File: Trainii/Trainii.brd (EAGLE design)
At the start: 50.8 x 71.1 mm, 31 parts, among them J1 apd, J2 left motor encoder, J3 right motor encoder, J4 line sensor 2, J5 line sensor 1, J6 ultrasonic, J7 left motor output, J8 right motor output, J9 lift motor output, U1 TPS61222DCKR, U2 BSS138

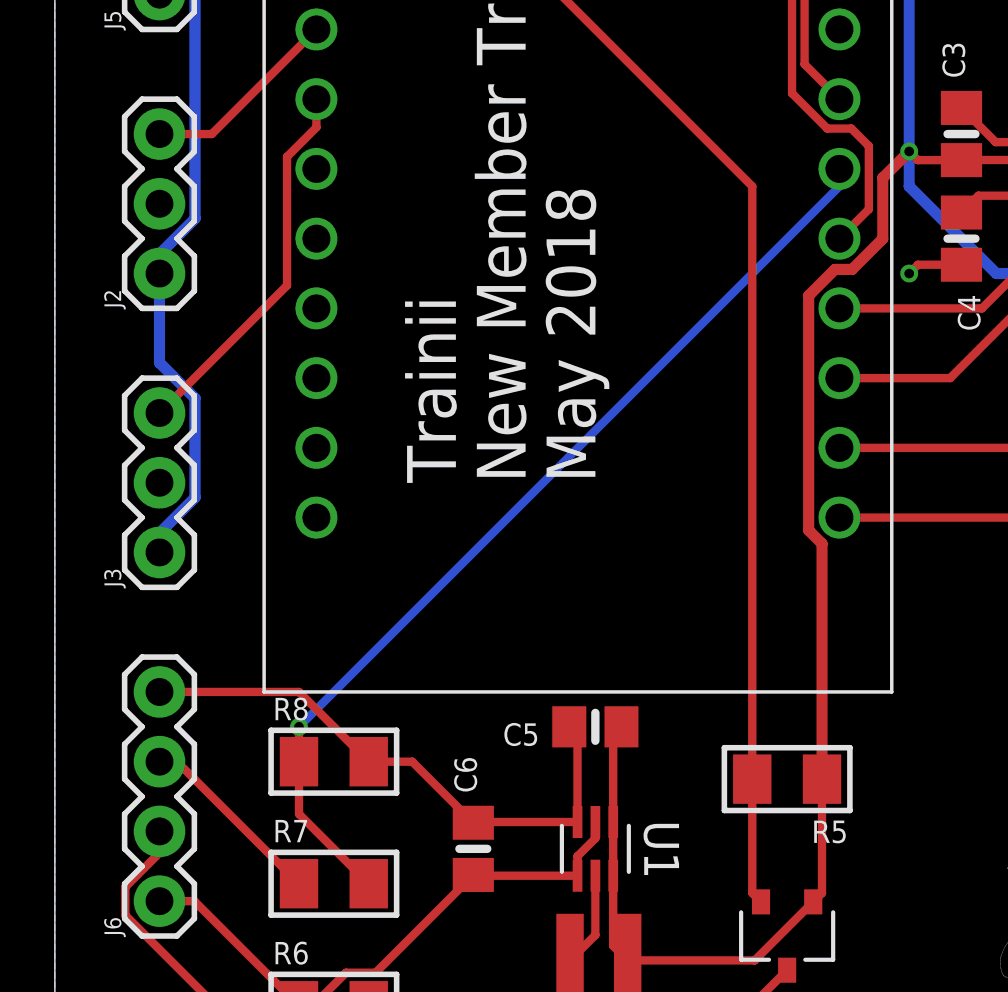
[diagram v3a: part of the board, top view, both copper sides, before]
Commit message: Fixes spacing between ECHO3.3 and R8
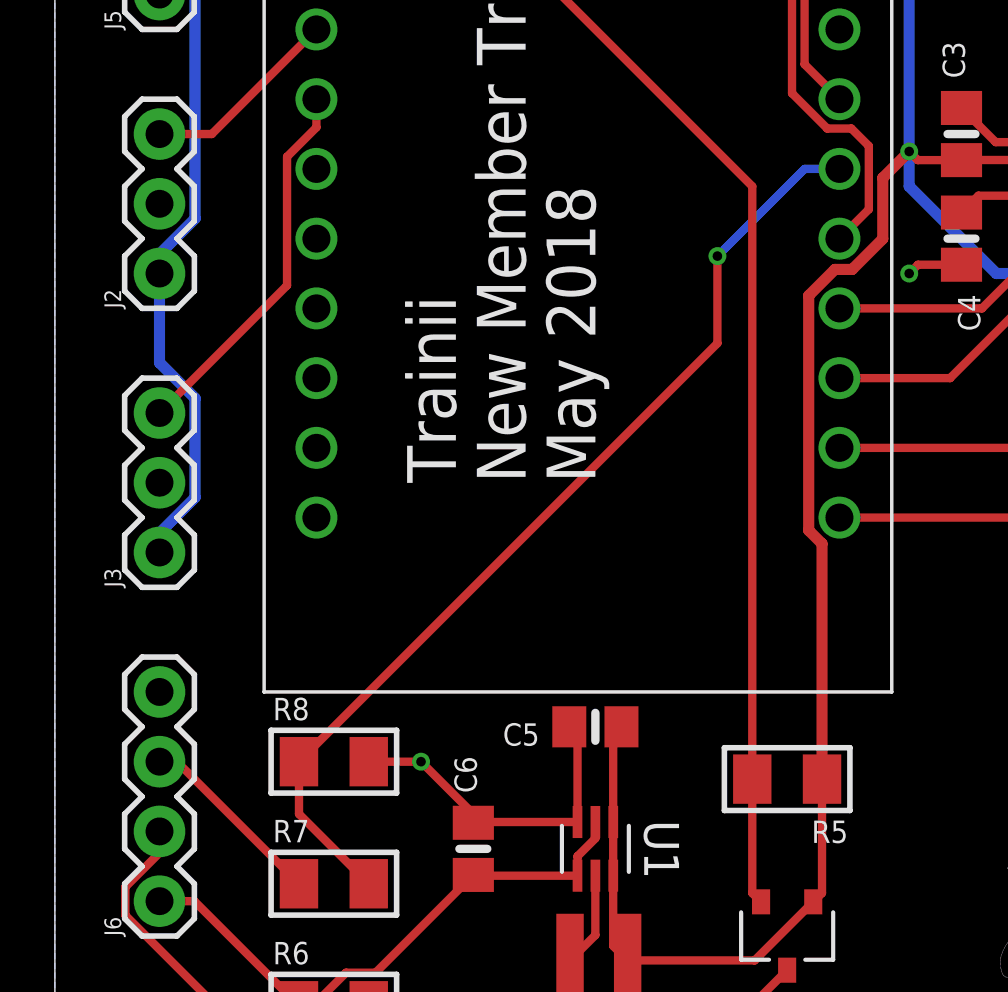
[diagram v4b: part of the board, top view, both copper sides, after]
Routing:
- net GND: track 55.1 -> 46.6 mm, vias 4 -> 5
- net ECHO3.3: track 35.2 -> 36.0 mm
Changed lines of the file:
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@@
 <wire x1="19.035" y1="15.5829" x2="19.035" y2="18.75" width="0.3048" layer="1"/>
 <wire x1="19.035" y1="18.75" x2="18.735" y2="19.05" width="0.3048" layer="1"/>
-<wire x1="15.24" y1="15.555" x2="13.015" y2="17.78" width="0.3048" layer="1"/>
-<wire x1="13.015" y1="17.78" x2="11.43" y2="17.78" width="0.3048" layer="1"/>
-<wire x1="11.43" y1="17.78" x2="8.89" y2="20.32" width="0.3048" layer="1"/>
-<wire x1="8.89" y1="20.32" x2="3.81" y2="20.32" width="0.3048" layer="1"/>
 <wire x1="39.37" y1="33.02" x2="39.37" y2="39.37" width="0.3048" layer="1"/>
 <wire x1="33.02" y1="56.2" x2="31.435" y2="56.2" width="0.3048" layer="1"/>
@@
 <wire x1="39.37" y1="62.865" x2="39.37" y2="66.04" width="0.3048" layer="1"/>
 <via x="39.37" y="62.865" extent="1-16" drill="0.35"/>
+<wire x1="11.43" y1="17.78" x2="13.335" y2="17.78" width="0.3048" layer="1"/>
+<via x="13.335" y="17.78" extent="1-16" drill="0.35"/>
+<wire x1="13.335" y1="17.78" x2="15.2679" y2="15.8471" width="0.3048" layer="1"/>
+<wire x1="15.2679" y1="15.8471" x2="15.2679" y2="15.5829" width="0.3048" layer="1"/>
 </signal>
 <signal name="N$3">
@@
 <wire x1="11.43" y1="13.335" x2="8.89" y2="15.875" width="0.3048" layer="1"/>
 <wire x1="8.89" y1="15.875" x2="8.89" y2="17.78" width="0.3048" layer="1"/>
-<wire x1="8.89" y1="17.78" x2="8.89" y2="19.05" width="0.3048" layer="1"/>
-<via x="8.89" y="19.05" extent="1-16" drill="0.35"/>
-<wire x1="8.89" y1="19.05" x2="28.575" y2="38.735" width="0.3048" layer="16"/>
-<wire x1="28.575" y1="38.735" x2="28.575" y2="39.37" width="0.3048" layer="16"/>
+<wire x1="8.89" y1="17.78" x2="24.13" y2="33.02" width="0.3048" layer="1"/>
+<wire x1="24.13" y1="33.02" x2="24.13" y2="36.195" width="0.3048" layer="1"/>
+<via x="24.13" y="36.195" extent="1-16" drill="0.35"/>
+<wire x1="24.13" y1="36.195" x2="27.305" y2="39.37" width="0.3048" layer="16"/>
+<wire x1="27.305" y1="39.37" x2="28.575" y2="39.37" width="0.3048" layer="16"/>
 </signal>
 <signal name="3V">

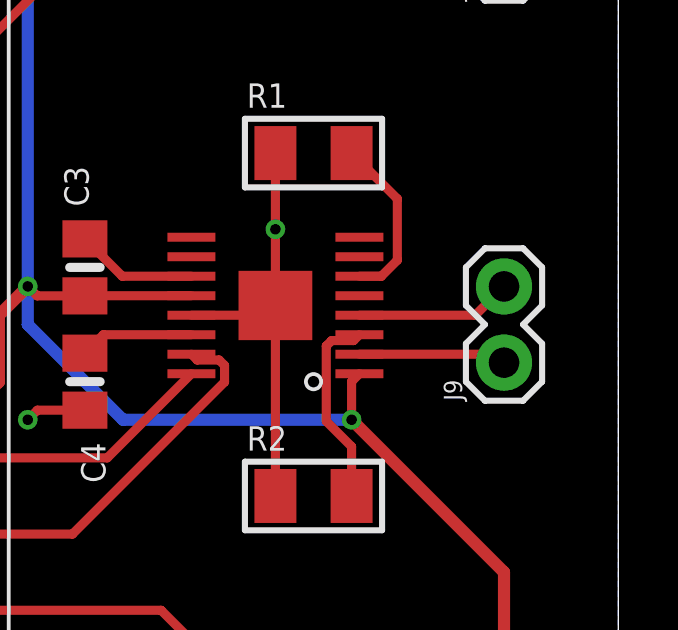
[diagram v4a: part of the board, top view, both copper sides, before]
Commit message: Fixes location of J9
It was slightly off of the 0.1" grid I tried to fit all of the connectors to.
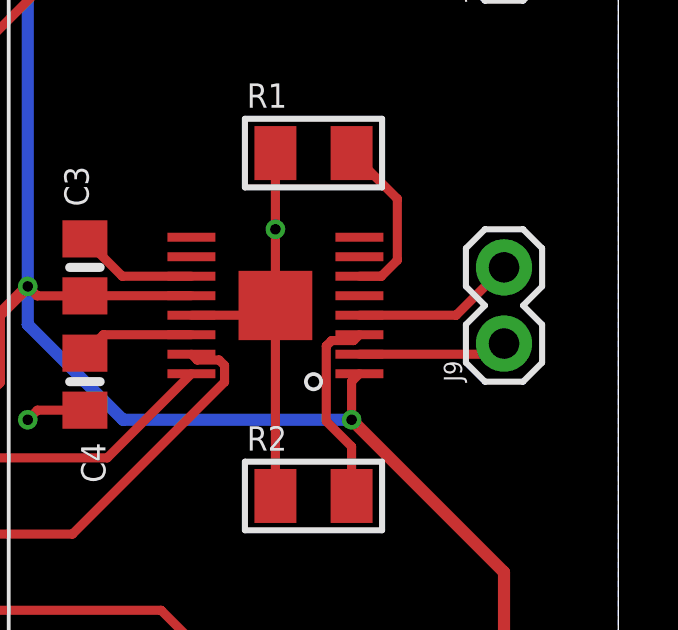
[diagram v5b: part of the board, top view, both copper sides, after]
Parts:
- moved J9 0.63 mm to (47.0, 38.1)
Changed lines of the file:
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@@
 <element name="J7" library="SparkFun-Connectors" library_urn="urn:adsk.eagle:library:513" package="1X02" package3d_urn="urn:adsk.eagle:package:38039/1" value="left motor output" x="46.99" y="50.8" rot="R90"/>
 <element name="J8" library="SparkFun-Connectors" library_urn="urn:adsk.eagle:library:513" package="1X02" package3d_urn="urn:adsk.eagle:package:38039/1" value="right motor output" x="46.99" y="58.42" rot="R90"/>
-<element name="J9" library="SparkFun-Connectors" library_urn="urn:adsk.eagle:library:513" package="1X02" package3d_urn="urn:adsk.eagle:package:38039/1" value="lift motor output" x="46.99" y="37.465" rot="R90"/>
+<element name="J9" library="SparkFun-Connectors" library_urn="urn:adsk.eagle:library:513" package="1X02" package3d_urn="urn:adsk.eagle:package:38039/1" value="lift motor output" x="46.99" y="38.1" rot="R90"/>
 <element name="MC2" library="Trainii" package="DRV8833" value="DRV8833" x="39.37" y="39.37" rot="R90"/>
 <element name="C3" library="microbuilder" package="0805-NO" value="0.1uF" x="33.02" y="40.64" rot="R90"/>
@@
 <contactref element="J9" pad="1"/>
 <contactref element="MC2" pad="AOUT1"/>
-<wire x1="42.17" y1="37.745" x2="46.71" y2="37.745" width="0.3048" layer="1"/>
-<wire x1="46.71" y1="37.745" x2="46.99" y2="37.465" width="0.3048" layer="1"/>
+<wire x1="42.17" y1="37.745" x2="46.635" y2="37.745" width="0.3048" layer="1"/>
+<wire x1="46.635" y1="37.745" x2="46.99" y2="38.1" width="0.3048" layer="1"/>
 </signal>
 <signal name="RIGHT_B">
@@
 <contactref element="MC2" pad="AOUT2"/>
 <contactref element="J9" pad="2"/>
-<wire x1="42.17" y1="39.045" x2="46.03" y2="39.045" width="0.3048" layer="1"/>
-<wire x1="46.03" y1="39.045" x2="46.99" y2="40.005" width="0.3048" layer="1"/>
+<wire x1="42.17" y1="39.045" x2="45.395" y2="39.045" width="0.3048" layer="1"/>
+<wire x1="45.395" y1="39.045" x2="46.99" y2="40.64" width="0.3048" layer="1"/>
 </signal>
 <signal name="RIGHT_0">

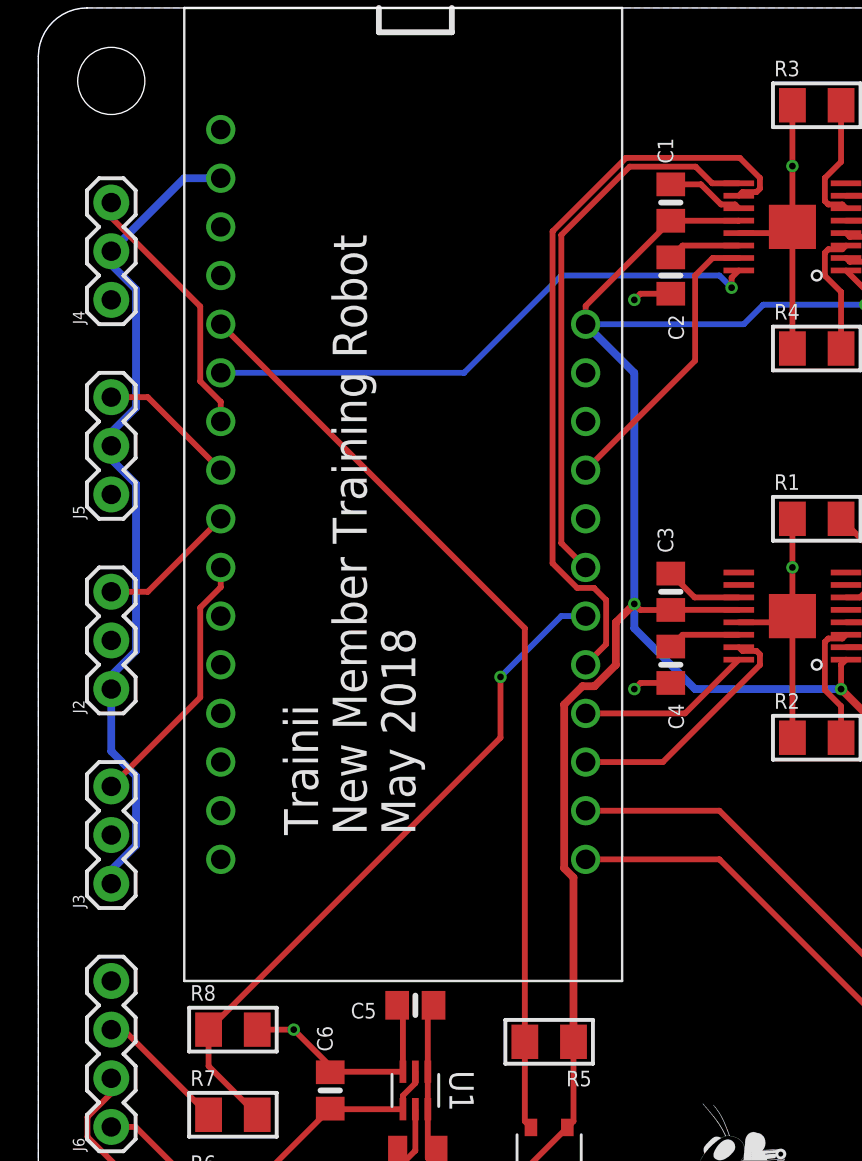
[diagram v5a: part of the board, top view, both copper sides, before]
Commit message: Fixes header spacing for the Huzzah ESP32 in Trainii.lbr
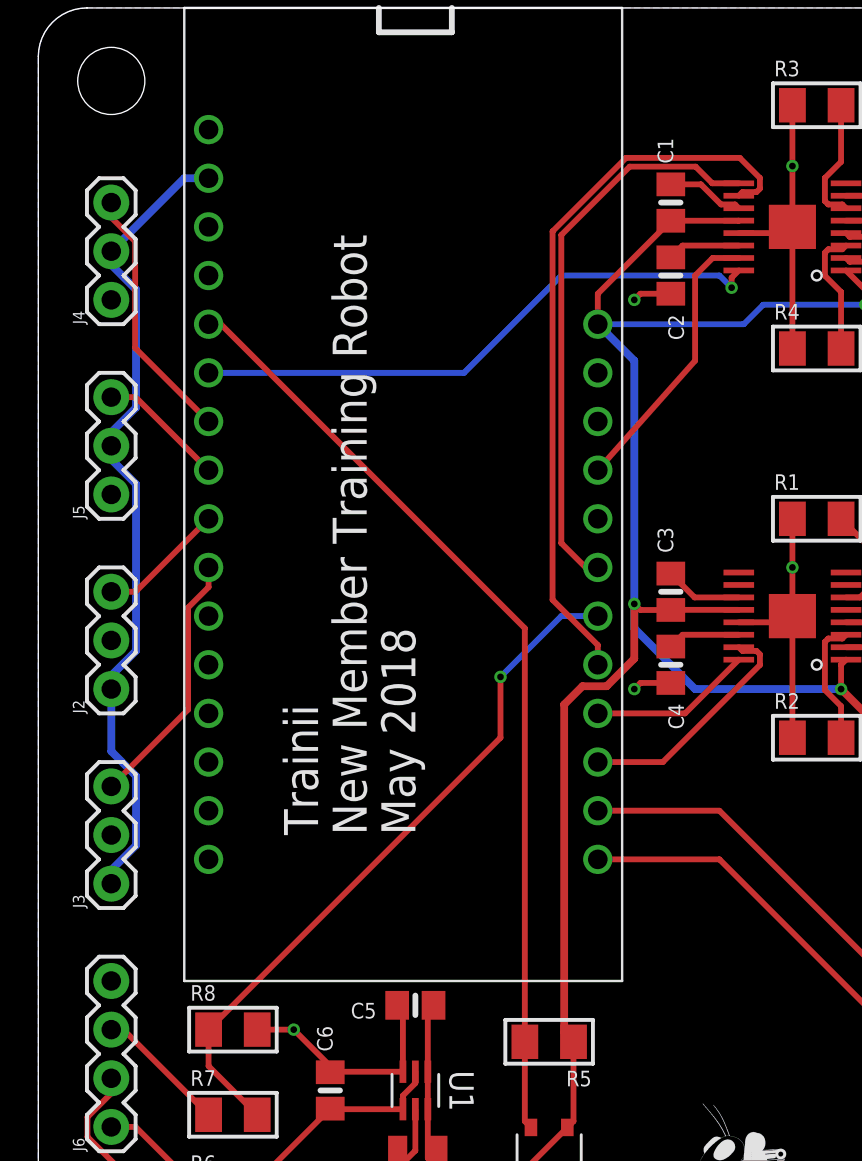
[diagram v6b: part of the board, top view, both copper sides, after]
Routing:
- net RIGHT_B: track 39.4 -> 38.3 mm
- net VCC: track 122.6 -> 121.8 mm
- net 3V: track 43.5 -> 42.9 mm
- net SDA: track 23.1 -> 22.5 mm
- net SCL: track 23.1 -> 22.5 mm
- net RIGHT_A: track 29.0 -> 29.6 mm
- net LIFT_B: track 13.0 -> 12.4 mm
- net LIFT_A: track 9.16 -> 8.52 mm
- net LEFT_A: track 30.1 -> 30.7 mm
- net TICK_LEFT: track 7.29 -> 6.66 mm
- net LINE_OUT_2: track 7.29 -> 6.66 mm
- net TRIG3.3: track 48.6 -> 49.3 mm
- net ECHO3.3: track 36.0 -> 36.6 mm
